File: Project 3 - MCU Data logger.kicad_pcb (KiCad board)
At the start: 2 copper layers, 31 parts, among them J1 Conn_01x04_Pin, J2 Conn_01x04_Pin, J3 Conn_01x09_Pin, J4 Conn_02x03_Odd_Even, U1 24AA02-OT, U2 24AA02-OT, U3 DS1337, U4 ATMEGA328P-AU, Y1 16MHz, Y2 32.678KHz

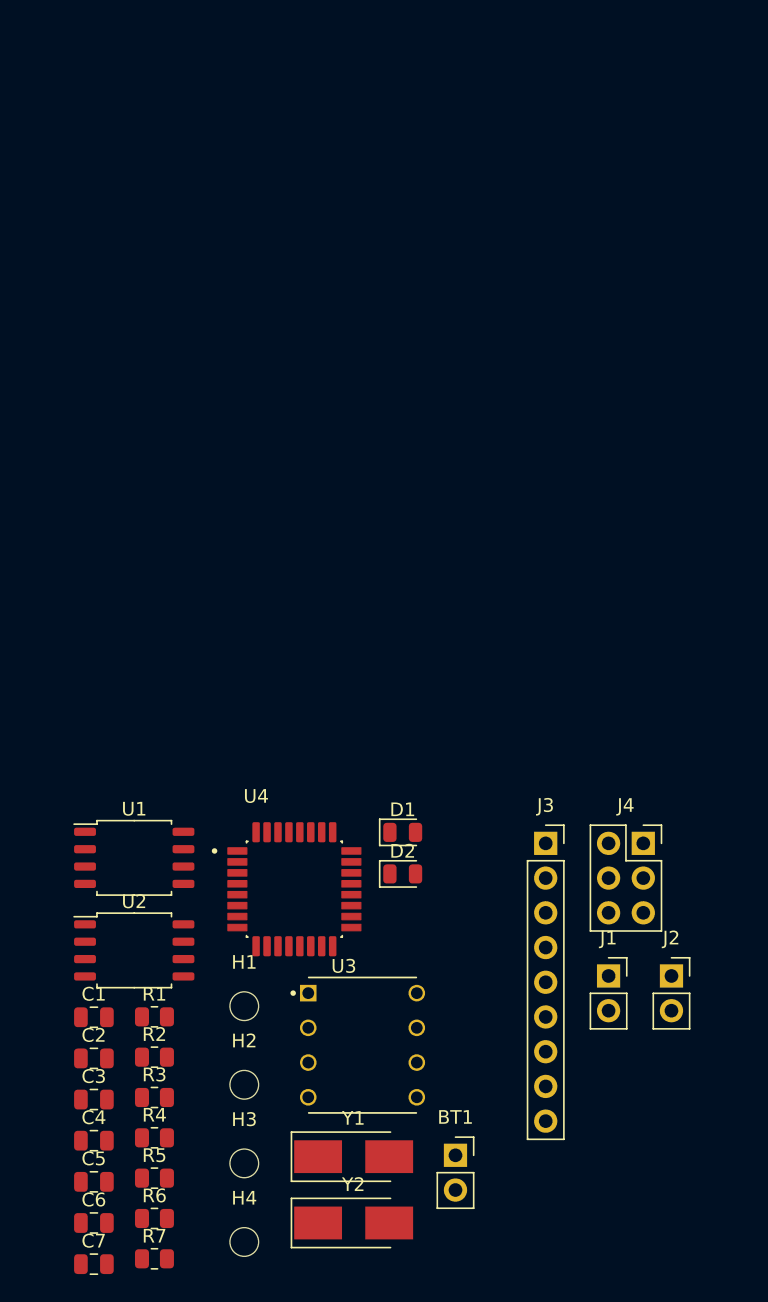
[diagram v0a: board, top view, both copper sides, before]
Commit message: added intial routing
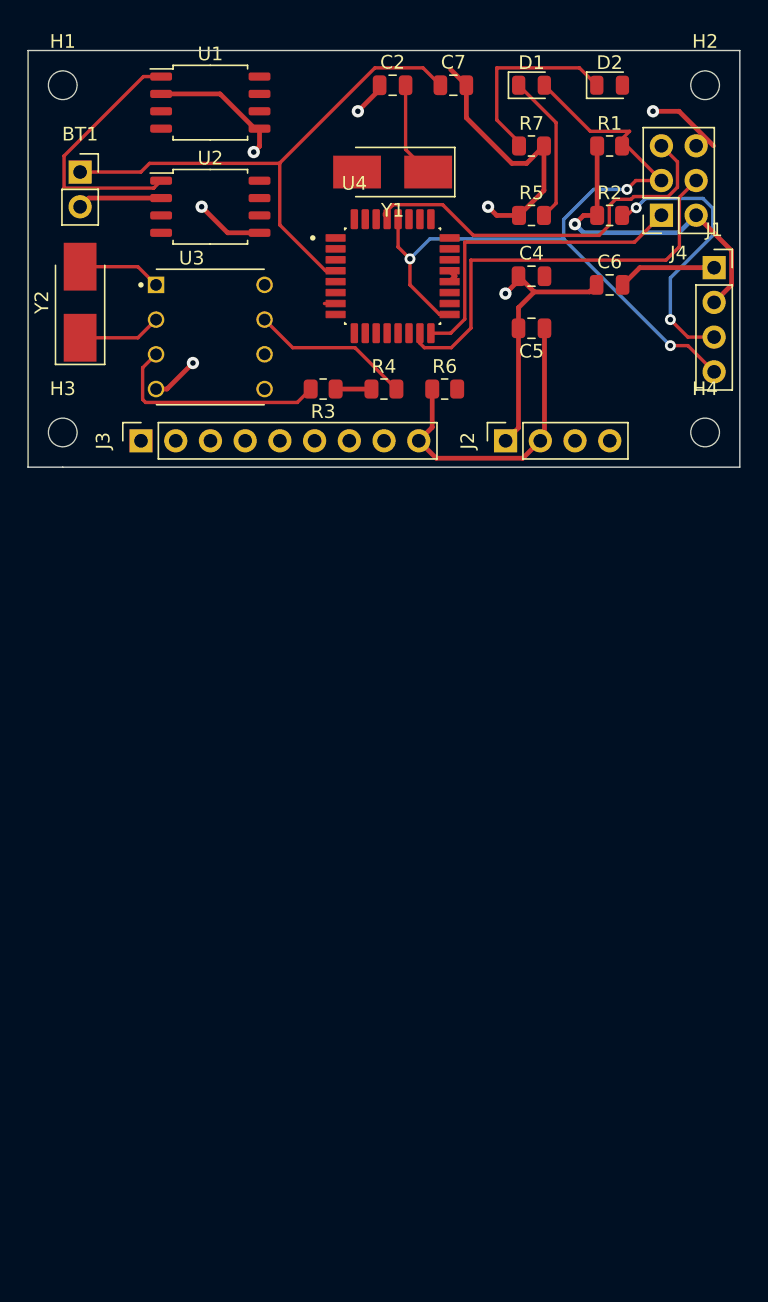
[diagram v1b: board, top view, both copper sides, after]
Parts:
- removed C1, C3: 0.1u, Capacitor_SMD:C_0805_2012Metric
- J1, J2: footprint Connector_PinSocket_2.54mm:PinSocket_1x02_P2.54mm_Vertical -> Connector_PinSocket_2.54mm:PinSocket_1x04_P2.54mm_Vertical
- moved C7 90.2 mm to (131.4, 33.0)
- moved R7 86.0 mm to (137.2, 37.5)
- moved H2 80.5 mm to (149.9, 33.0)
- moved C6 78.3 mm to (142.9, 47.6)
- moved BT1 77.0 mm to (104.1, 39.4)
- moved R5 75.6 mm to (137.2, 42.5)
- moved C2 74.5 mm to (127.0, 33.0)
- moved Y1 72.1 mm to (127.0, 39.4), turned to 180 degrees
- moved R1 71.9 mm to (142.9, 37.5)
- moved C4 70.9 mm to (137.2, 47.0)
- moved Y2 70.3 mm to (104.1, 48.9), turned to 90 degrees
- moved C5 70.2 mm to (137.2, 50.8), turned to 180 degrees
- moved R2 70.0 mm to (142.9, 42.5)
- moved H1 68.7 mm to (102.9, 33.0)
- moved H4 68.1 mm to (149.9, 58.4)
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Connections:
- BT1 pad 1: unconnected-(BT1-+-Pad1) -> Net-(BT1-+)
- BT1 pad 2: unconnected-(BT1---Pad2) -> GND
- C2 pad 1: unconnected-(C2-Pad1) -> GND
- C2 pad 2: unconnected-(C2-Pad2) -> Net-(U4-PB6)
- C4 pad 1: unconnected-(C4-Pad1) -> GND
- C4 pad 2: unconnected-(C4-Pad2) -> Net-(U4-PB7)
- C5 pad 1: unconnected-(C5-Pad1) -> VCC
- C5 pad 2: unconnected-(C5-Pad2) -> GND
- C6 pad 1: unconnected-(C6-Pad1) -> GND
- C6 pad 2: unconnected-(C6-Pad2) -> GND
- C7 pad 1: unconnected-(C7-Pad1) -> Net-(BT1-+)
- C7 pad 2: unconnected-(C7-Pad2) -> GND
- D1 pad 1: unconnected-(D1-K-Pad1) -> Net-(D1-K)
- D1 pad 2: unconnected-(D1-A-Pad2) -> /SCL
- D2 pad 1: unconnected-(D2-K-Pad1) -> Net-(D2-K)
- D2 pad 2: unconnected-(D2-A-Pad2) -> Net-(BT1-+)
- J1 pad 1: unconnected-(J1-Pin_1-Pad1) -> GND
- J1 pad 2: unconnected-(J1-Pin_2-Pad2) -> VCC
- J2 pad 1: unconnected-(J2-Pin_1-Pad1) -> GND
- J2 pad 2: unconnected-(J2-Pin_2-Pad2) -> VCC
- J3 pad 1: unconnected-(J3-Pin_1-Pad1) -> /D2
- J3 pad 2: unconnected-(J3-Pin_2-Pad2) -> /D3
- J3 pad 3: unconnected-(J3-Pin_3-Pad3) -> /D4
- J3 pad 4: unconnected-(J3-Pin_4-Pad4) -> /D5
- J3 pad 5: unconnected-(J3-Pin_5-Pad5) -> /D6
- J3 pad 6: unconnected-(J3-Pin_6-Pad6) -> /D7
- J3 pad 7: unconnected-(J3-Pin_7-Pad7) -> /D8
- J3 pad 8: unconnected-(J3-Pin_8-Pad8) -> GND
- J3 pad 9: unconnected-(J3-Pin_9-Pad9) -> VCC
- J4 pad 1: unconnected-(J4-Pin_1-Pad1) -> /MISO
- J4 pad 2: unconnected-(J4-Pin_2-Pad2) -> VCC
- J4 pad 3: unconnected-(J4-Pin_3-Pad3) -> /SCL
- J4 pad 4: unconnected-(J4-Pin_4-Pad4) -> /MOSI
- J4 pad 5: unconnected-(J4-Pin_5-Pad5) -> /RESET
- J4 pad 6: unconnected-(J4-Pin_6-Pad6) -> GND
- R1 pad 1: unconnected-(R1-Pad1) -> VCC
- R1 pad 2: unconnected-(R1-Pad2) -> /SCL
- R2 pad 1: unconnected-(R2-Pad1) -> VCC
- R2 pad 2: unconnected-(R2-Pad2) -> /SDA
- R3 pad 1: unconnected-(R3-Pad1) -> VCC
- R3 pad 2: unconnected-(R3-Pad2) -> Net-(U3-#INTA)
- R4 pad 1: unconnected-(R4-Pad1) -> VCC
- R4 pad 2: unconnected-(R4-Pad2) -> Net-(U3-SQW/#INTB)
- R5 pad 1: unconnected-(R5-Pad1) -> GND
- R5 pad 2: unconnected-(R5-Pad2) -> Net-(D1-K)
- R6 pad 1: unconnected-(R6-Pad1) -> VCC
- R6 pad 2: unconnected-(R6-Pad2) -> /RESET
- R7 pad 1: unconnected-(R7-Pad1) -> Net-(D2-K)
- R7 pad 2: unconnected-(R7-Pad2) -> GND
- U1 pad 1: unconnected-(U1-SCL-Pad1) -> /SCL
- U1 pad 2: unconnected-(U1-V_{SS}-Pad2) -> GND
- U1 pad 3: unconnected-(U1-SDA-Pad3) -> /SDA
- U1 pad 4: unconnected-(U1-V_{CC}-Pad4) -> VCC
- U1 pad 5: unconnected-(U1-WP-Pad5) -> GND
- U2 pad 1: unconnected-(U2-SCL-Pad1) -> /SCL
- U2 pad 2: unconnected-(U2-V_{SS}-Pad2) -> GND
- U2 pad 3: unconnected-(U2-SDA-Pad3) -> /SDA
- U2 pad 4: unconnected-(U2-V_{CC}-Pad4) -> VCC
- U2 pad 5: unconnected-(U2-WP-Pad5) -> GND
- U3 pad 1: unconnected-(U3-X1-Pad1) -> Net-(U3-X1)
- U3 pad 2: unconnected-(U3-X2-Pad2) -> Net-(U3-X2)
- U3 pad 3: unconnected-(U3-#INTA-Pad3) -> Net-(U3-#INTA)
- U3 pad 4: unconnected-(U3-GND-Pad4) -> GND
- U3 pad 5: unconnected-(U3-SDA-Pad5) -> /SDA
- U3 pad 6: unconnected-(U3-SCL-Pad6) -> /SCL
- U3 pad 7: unconnected-(U3-SQW/#INTB-Pad7) -> Net-(U3-SQW/#INTB)
- U3 pad 8: unconnected-(U3-VCC-Pad8) -> VCC
- U4 pad 1: unconnected-(U4-PD3-Pad1) -> /D3
- U4 pad 10: unconnected-(U4-PD6-Pad10) -> /D6
- U4 pad 11: unconnected-(U4-PD7-Pad11) -> /D7
- U4 pad 12: unconnected-(U4-PB0-Pad12) -> /D8
- U4 pad 15: unconnected-(U4-PB3-Pad15) -> /MOSI
- U4 pad 16: unconnected-(U4-PB4-Pad16) -> /MISO
- U4 pad 17: unconnected-(U4-PB5-Pad17) -> /SCL
- U4 pad 18: unconnected-(U4-AVCC-Pad18) -> Net-(BT1-+)
- U4 pad 2: unconnected-(U4-PD4-Pad2) -> /D4
- U4 pad 20: unconnected-(U4-AREF-Pad20) -> GND
- U4 pad 21: Net-(U4-GND-Pad21) -> GND
- U4 pad 27: unconnected-(U4-PC4-Pad27) -> /SDA
- U4 pad 28: unconnected-(U4-PC5-Pad28) -> /SCL
- U4 pad 29: unconnected-(U4-PC6/~{RESET}-Pad29) -> /RESET
- U4 pad 3: Net-(U4-GND-Pad21) -> GND
- U4 pad 30: unconnected-(U4-PD0-Pad30) -> /RX
- U4 pad 31: unconnected-(U4-PD1-Pad31) -> /TX
- U4 pad 32: unconnected-(U4-PD2-Pad32) -> /D2
- U4 pad 4: Net-(U4-VCC-Pad4) -> Net-(BT1-+)
- U4 pad 5: Net-(U4-GND-Pad21) -> GND
- U4 pad 6: Net-(U4-VCC-Pad4) -> unconnected-(U4-VCC-Pad6)
- U4 pad 7: unconnected-(U4-PB6-Pad7) -> Net-(U4-PB6)
- U4 pad 8: unconnected-(U4-PB7-Pad8) -> Net-(U4-PB7)
- U4 pad 9: unconnected-(U4-PD5-Pad9) -> /D5
- Y1 pad 1: unconnected-(Y1-Pad1) -> Net-(U4-PB6)
- Y1 pad 2: unconnected-(Y1-Pad2) -> Net-(U4-PB7)
- Y2 pad 1: unconnected-(Y2-Pad1) -> Net-(U3-X2)
- Y2 pad 2: unconnected-(Y2-Pad2) -> Net-(U3-X1)
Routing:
- net GND: track 0.00 -> 81.1 mm, vias 0 -> 7
- net /SCL: track 0.00 -> 77.6 mm, vias 0 -> 3
- net VCC: track 0.00 -> 49.7 mm, vias 0 -> 1
- net Net-(BT1-+): track 0.00 -> 40.0 mm
- net /MOSI: track 0.00 -> 31.2 mm
- net /RESET: track 0.00 -> 28.9 mm
- net /MISO: track 0.00 -> 23.7 mm
- net /SDA: track 0.00 -> 20.7 mm, vias 0 -> 2
- net Net-(U3-#INTA): track 0.00 -> 16.5 mm
- net Net-(D2-K): track 0.00 -> 14.2 mm
- net Net-(U3-SQW/#INTB): track 0.00 -> 11.7 mm
- net Net-(D1-K): track 0.00 -> 11.0 mm
- net Net-(U4-PB6): track 0.00 -> 7.85 mm
- net Net-(U3-X2): track 0.00 -> 6.11 mm
- net Net-(U3-X1): track 0.00 -> 6.11 mm
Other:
- board outline added: 52.1 x 30.5 mm

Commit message: added routing
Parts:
- moved C4 1.91 mm to (137.2, 45.1)
- turned C2 to 180 degrees
- turned R6 to 180 degrees
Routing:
- net GND: track 81.1 -> 188.8 mm, vias 7 -> 15
- net Net-(BT1-+): track 40.0 -> 129.5 mm, vias 0 -> 3
- net /SDA: track 20.7 -> 93.8 mm, vias 2 -> 7
- net VCC: track 49.7 -> 98.4 mm, vias 1 -> 9
- net /SCL: track 77.6 -> 118.1 mm, vias 3 -> 4
- net Net-(U4-PB7): track 0.00 -> 37.4 mm, vias 0 -> 3
- net /TX: track 0.00 -> 30.0 mm, vias 0 -> 1
- net /RESET: track 28.9 -> 58.8 mm, vias 0 -> 2
- net /D2: track 0.00 -> 27.0 mm, vias 0 -> 1
- net /RX: track 0.00 -> 23.9 mm, vias 0 -> 1
- net /D3: track 0.00 -> 23.4 mm, vias 0 -> 1
- net /D4: track 0.00 -> 21.5 mm, vias 0 -> 1
- net Net-(U4-PB6): track 7.85 -> 27.5 mm, vias 0 -> 2
- net /D5: track 0.00 -> 11.6 mm, vias 0 -> 2
- net /D8: track 0.00 -> 11.1 mm
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
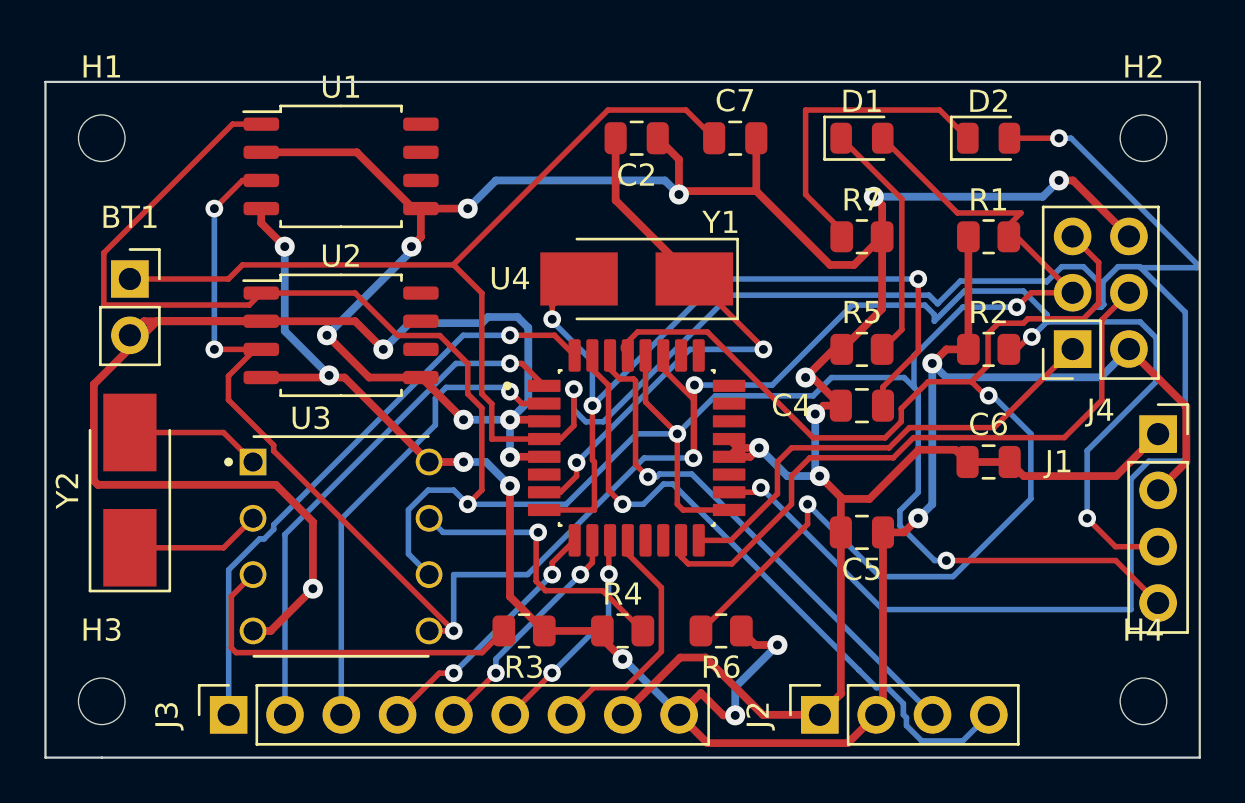
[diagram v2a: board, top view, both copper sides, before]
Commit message: add silkscreen and improve text
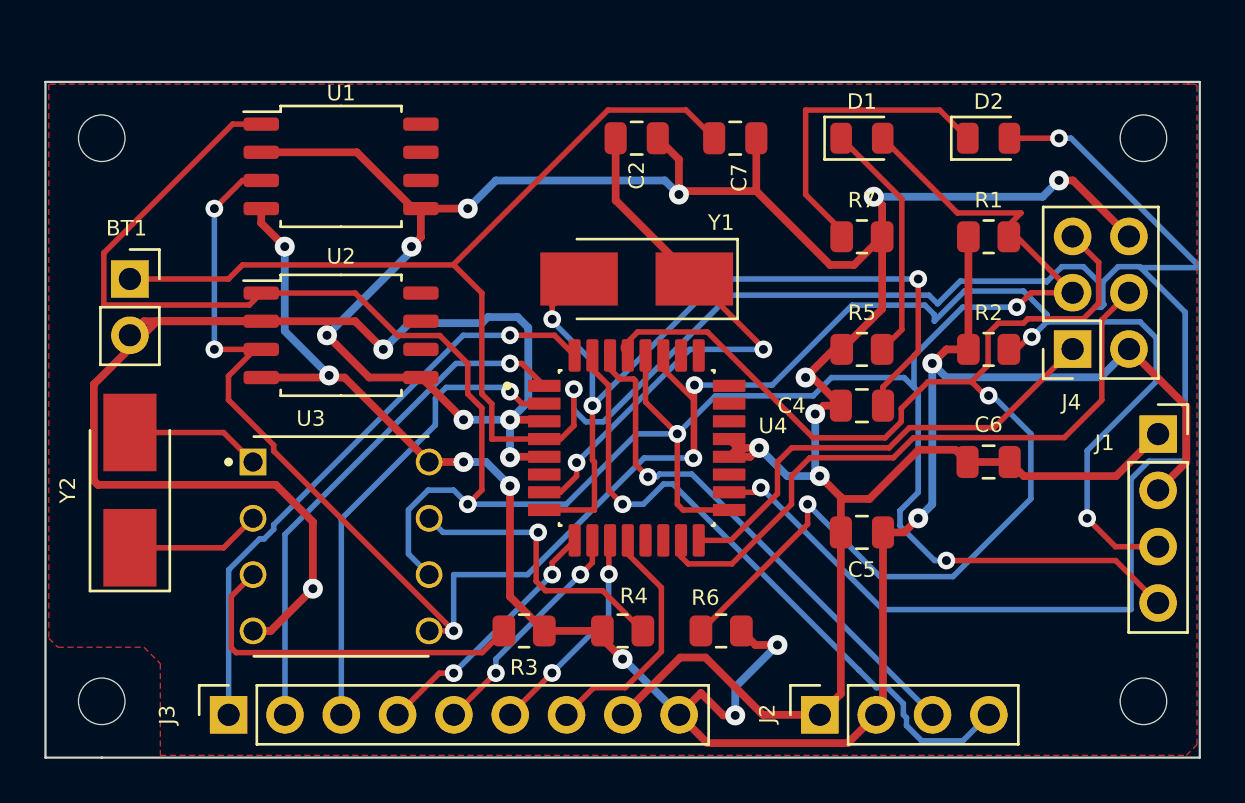
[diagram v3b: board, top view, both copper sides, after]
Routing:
- added copper zone on F.Cu, net GND

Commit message: add text and graphics
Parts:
- added REF**: KiCad-Logo2_12mm_SilkScreen, Symbol:KiCad-Logo2_12mm_SilkScreen, B.Cu at (126.2, 43.2)
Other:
- board text added: "Data logger with ATMega328P"
- board text added: "ICSP RESET | GND SC | MOSI MISO | VCC"

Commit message: add 3d model
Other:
- board text added: "- 2Mbit EEPRROM - RTC - I2C, SPI, GPIOs"
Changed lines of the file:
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@@
   (gr_line (start 100.33 30.48) (end 152.4 30.48)
     (stroke (width 0.1) (type default)) (layer "Edge.Cuts"))
-  (gr_text "Data logger with ATMega328P" (at 141.1224 32.1818 180) (layer "B.SilkS")
-    (effects (font (size 1.5 1.5) (thickness 0.3) bold) (justify left bottom))
+  (gr_text "Data logger with ATMega328P" (at 143.51 37.1602) (layer "B.SilkS")
+    (effects (font (size 1.5 1.5) (thickness 0.3) bold) (justify left bottom mirror))
+  )
+  (gr_text "- 2Mbit EEPRROM\n- RTC\n- I2C, SPI, GPIOs" (at 146.8882 59.309) (layer "B.SilkS")
+    (effects (font (size 1.5 0.8) (thickness 0.2) bold) (justify left bottom mirror))
   )
   (gr_text "	ICSP\nRESET | GND\nSC    | MOSI\nMISO  | VCC" (at 142.3416 55.8292) (layer "F.SilkS")
